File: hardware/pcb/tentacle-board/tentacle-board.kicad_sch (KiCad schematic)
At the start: 36 parts, among them IC1 W25Q32JVZPIQ, J1 DEBUG, J2 UART0, J3 Conn_01x02, J4 Conn_01x05, J7 Conn_01x05, J8 Conn_01x05, U1 NCP1117-3.3_SOT223, U3 RP2040, Y1 ABM8-12.000MHZ-20-B1U-T

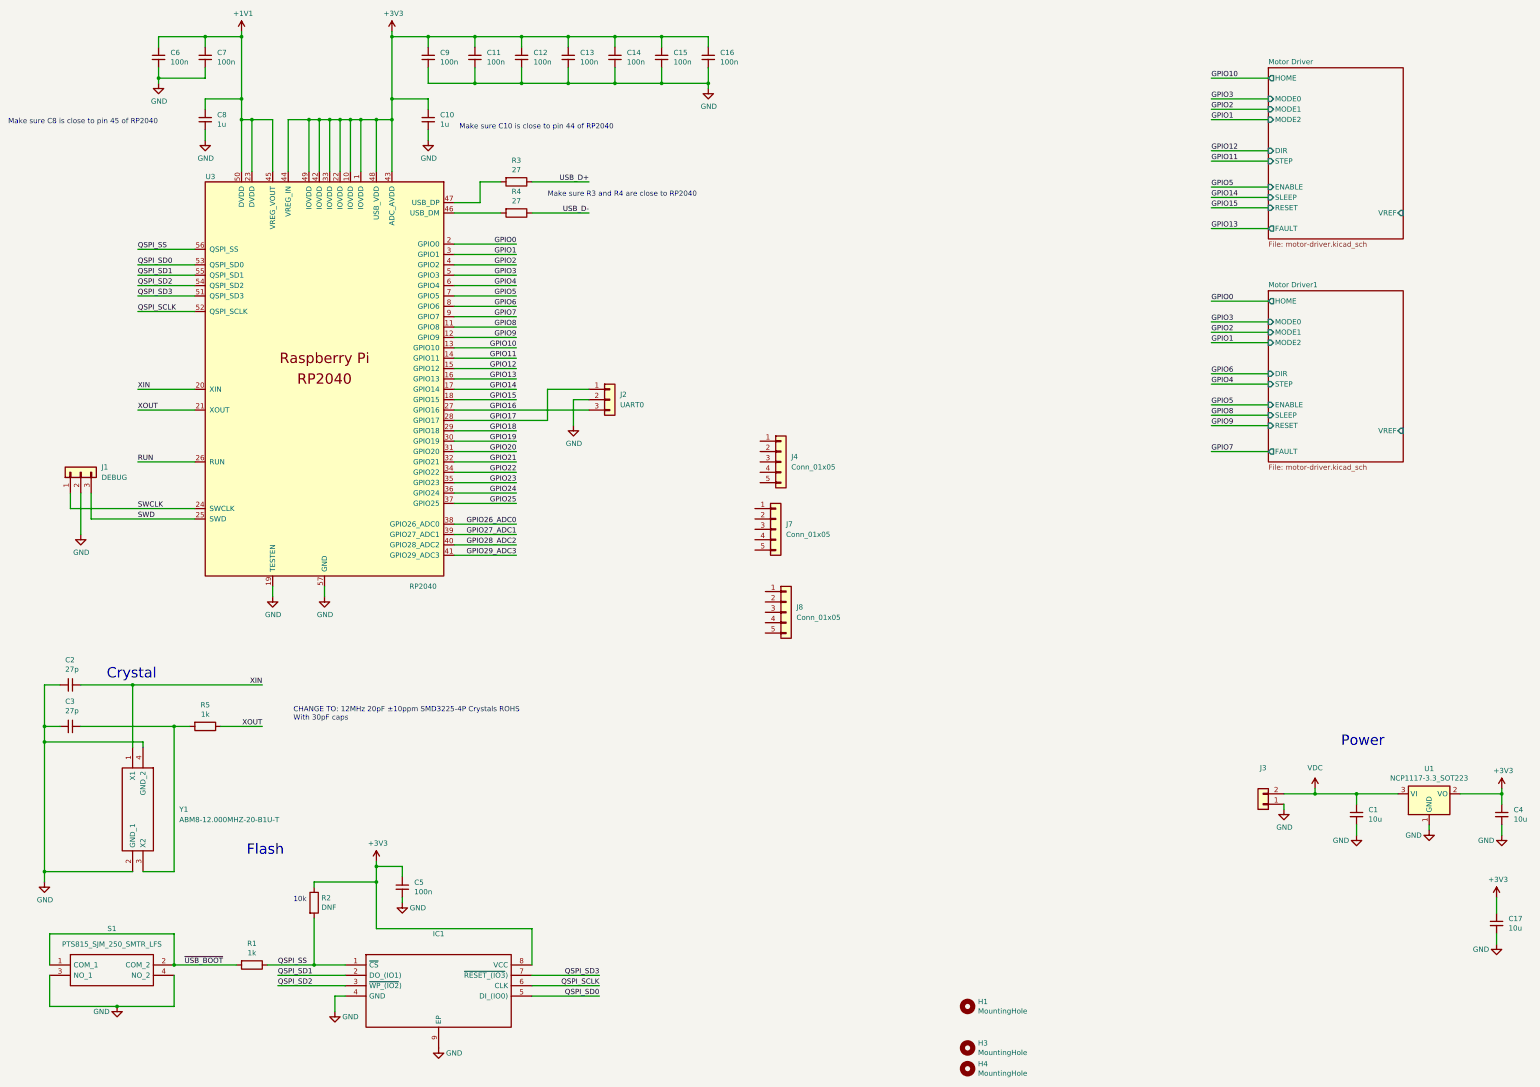
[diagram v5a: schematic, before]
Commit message: Finished component & trace layout
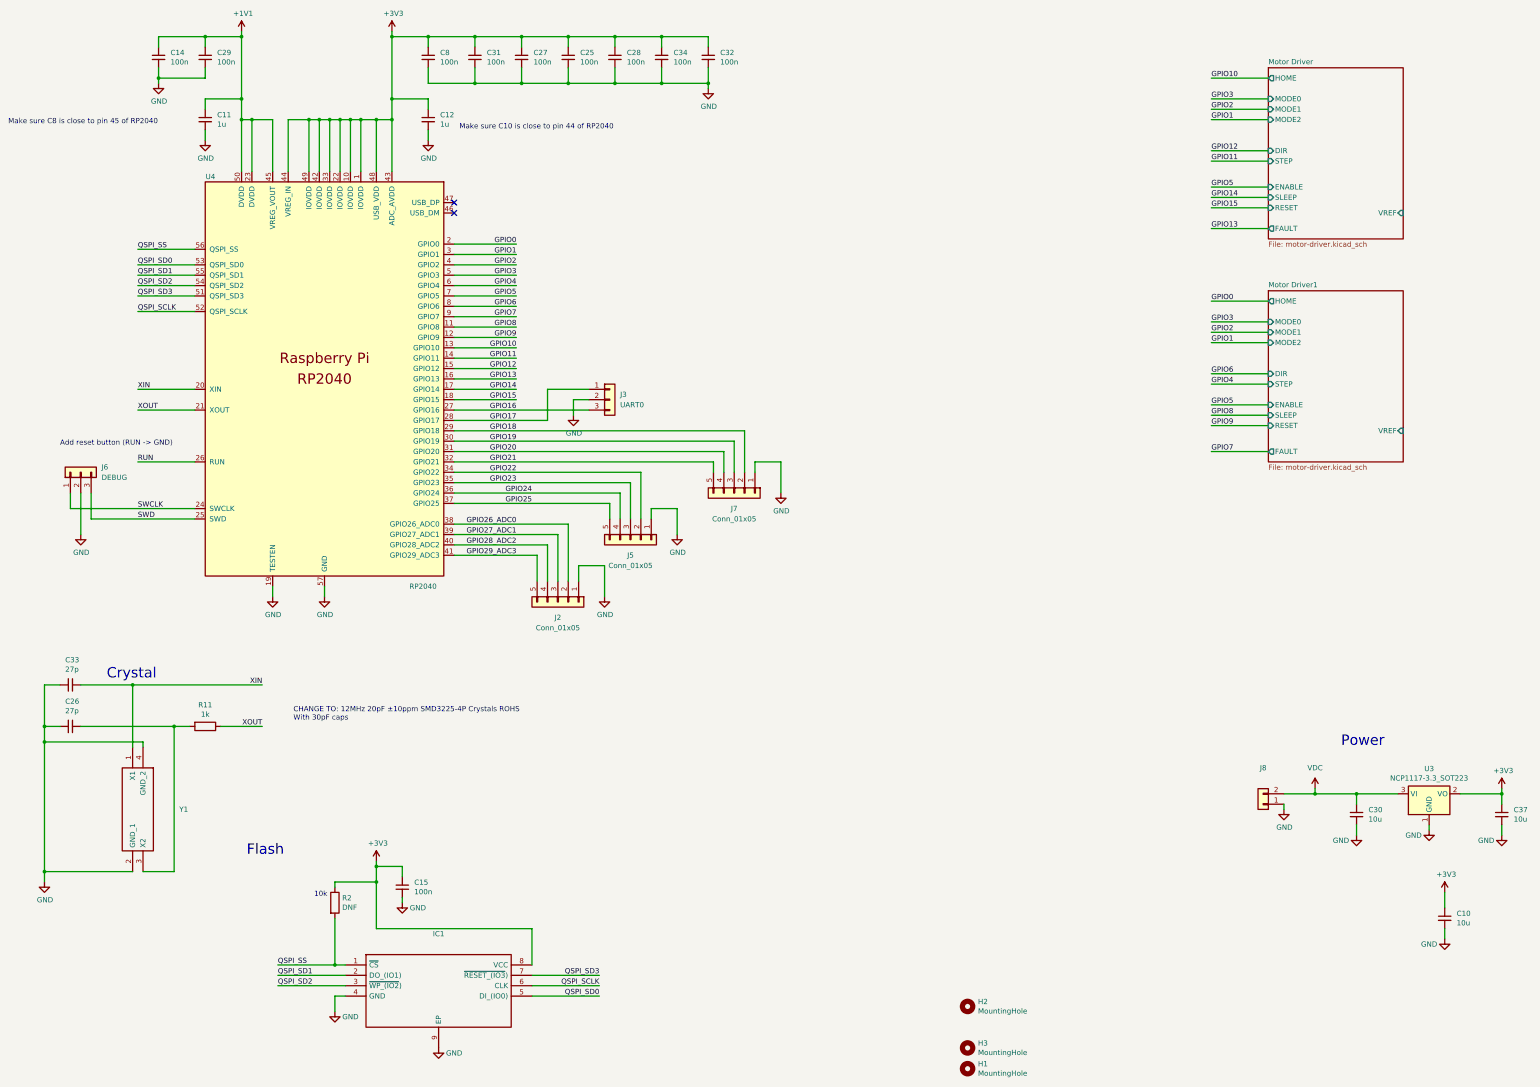
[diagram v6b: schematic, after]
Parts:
- removed R1: 1k, Capacitor_SMD:C_0402_1005Metric, symbol Device:R
- removed R3, R4: 27, Capacitor_SMD:C_0402_1005Metric, symbol Device:R
- removed S1: PTS815_SJM_250_SMTR_LFS, tentacle-board:PTS815SJM250SMTRLFS, symbol PTS815_SJM_250_SMTR_LFS:PTS815_SJM_250_SMTR_LFS
- IC1: footprint SON127P600X500X80-9N-D -> tentacle-board:SON127P600X500X80-9N-D
- Y1: footprint ABM810000MHZ12D2W -> tentacle-board:ABM810000MHZ12D2W
- renumbered C17 to C10, C8 to C11, C10 to C12, C6 to C14, C5 to C15, C13 to C25, C3 to C26, C12 to C27, C14 to C28, C7 to C29, C1 to C30, C11 to C31, C16 to C32, C2 to C33, C15 to C34, C4 to C37, C9 to C8, H4 to H1, H1 to H2, J4 to J2, J2 to J3, J7 to J5, J1 to J6, J8 to J7, J3 to J8, R5 to R11, U1 to U3, U3 to U4
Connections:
- net GND: now also J2.1 (Pin_1), J5.1 (Pin_1), J7.1 (Pin_1)
- net GPIO18: now also J7.2 (Pin_2)
- net GPIO19: now also J7.3 (Pin_3)
- net GPIO20: now also J7.4 (Pin_4)
- net GPIO21: now also J7.5 (Pin_5)
- net GPIO22: now also J5.2 (Pin_2)
- net GPIO23: now also J5.3 (Pin_3)
- net GPIO24: now also J5.4 (Pin_4)
- net GPIO25: now also J5.5 (Pin_5)
- net GPIO26_ADC0: now also J2.2 (Pin_2)
- net GPIO27_ADC1: now also J2.3 (Pin_3)
- net GPIO28_ADC2: now also J2.4 (Pin_4)
- net GPIO29_ADC3: now also J2.5 (Pin_5)
- no-connect marks 0 -> 2
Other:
- note added: "Add reset button (RUN -> GND)"
- note removed: "Make sure R3 and R4 are close to RP2040"
- moved on the sheet: C10, J2, J5, J7, R2

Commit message: Finished v1 and created manufacturing outputs
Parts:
- removed R2: DNF, Capacitor_SMD:C_0402_1005Metric, symbol Device:R
- added FID1, FID2, FID3: Fiducial, Fiducial:Fiducial_0.5mm_Mask1mm, symbol Mechanical:Fiducial
- added R13: 1.5k, Resistor_SMD:R_0402_1005Metric_Pad0.72x0.64mm_HandSolder, symbol Device:R_Small
- added R2: 10k, Resistor_SMD:R_0402_1005Metric, symbol Device:R_Small
- added VR1: TC33X-2-103E, TC33X2503E, symbol TC33X-2-103E:TC33X-2-103E
- C10, C30, C37: value 10u -> 10uF; LCSC # (none) -> C15850; Mfr # (none) -> CL21A106KAYNNNE; Mouser # (none) -> 187-CL21A106KAYNNNE
- C11, C12: value 1u -> 1uF; LCSC # (none) -> C107372; Mfr # (none) -> CL05A105KQ5NNNC; Mouser # (none) -> 187-CL05A105KQ5NNNC
- C14, C15, C25, C27, C28, C29, C31, C32, C34, C8: value 100n -> 100nF; LCSC # (none) -> C60474; Mfr # (none) -> CC0402KRX7R7BB104; Mouser # (none) -> 603-CC402KRX7R7BB104
- C26, C33: value 27p -> 30pF; LCSC # (none) -> C107004; Mfr # (none) -> CC0402JRNPO9BN300; Mouser # (none) -> 603-CC402JRNPO9BN300
- J2: value Conn_01x05 -> AUX2
- J5: value Conn_01x05 -> AUX1
- J7: value Conn_01x05 -> CTRL
- R11: LCSC # (none) -> C11702; Mfr # (none) -> 0402WGF1001TCE; Mouser # (none) -> 303-0402WGF1001TCE
- U3: LCSC # (none) -> C2902118; Mfr # (none) -> NCP1117IST18T3G; Mouser # (none) -> 863-NCP1117IST18T3G
- U4: LCSC # (none) -> C2040
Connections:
- net +3V3: now also R13.2, R2.1, VR1.3 (CW)
- net GND: now also VR1.1 (CCW)
- net GPIO18: no longer J7.2 (Pin_2)
- net Motor Driver A/VREF: now also VR1.2 (WIPER)
- net QSPI_SS: now also R2.2
- net RUN: now also J7.2 (Pin_2), R13.1
- no-connect marks 2 -> 3
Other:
- sheet Motor Driver renamed Motor Driver B
- sheet Motor Driver1 renamed Motor Driver A
- note removed: "10k"
- note removed: "Add reset button (RUN -> GND)"
- note removed: "CHANGE TO: 12MHz 20pF ±10ppm SMD3225-4P Crystals ROHS With 30pF caps"
- company: Raspberry Pi (Trading) Ltd -> Squeaky Robot
- title: RP2040 Minimal Design Example -> Tentacle Controller Board
- moved on the sheet: H1, H3
